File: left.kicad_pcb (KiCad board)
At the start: 2 copper layers, 140 x 27 mm, 11 parts, among them J1 FFC_Connector_13P

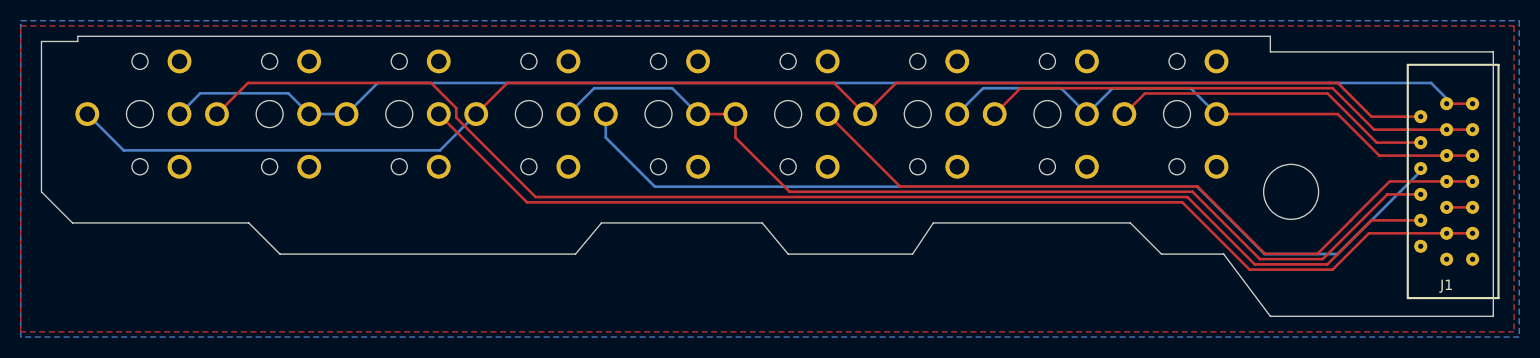
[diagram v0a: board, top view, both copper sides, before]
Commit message: Increase ffc connector hole size to 0.6 mm
The wires on the connector actually measure up to 0.57 mm.
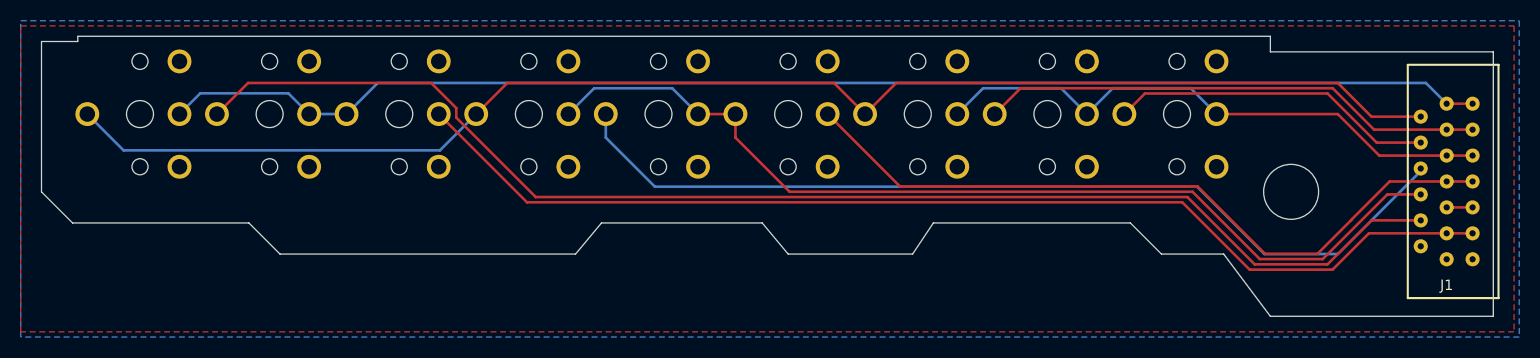
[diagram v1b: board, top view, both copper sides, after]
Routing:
- net Net-(ESC1-Pad2): track 128.9 -> 128.4 mm
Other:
- board text added: "V1.2 2022-04-30"
- board text removed: "V1.1 2022-04-22"
